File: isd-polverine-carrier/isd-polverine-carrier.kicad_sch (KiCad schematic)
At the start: 0 parts

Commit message: update: isd-polverine-carrier/sch (add battery protection circuit)
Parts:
- added C1: 0.1µF, symbol Device:C
- added C2: 10µF, symbol Device:C
- added F1: Fuse, symbol Device:Fuse
- added J1: BATT, Connector_JST:JST_PH_S2B-PH-K_1x02_P2.00mm_Horizontal, symbol Connector:Conn_01x02_Pin
- added Q1: Q_Dual_NMOS_S1G1D2S2G2D1, Package_SO:TSOP-6_1.65x3.05mm_P0.95mm, symbol Transistor_FET:Q_Dual_NMOS_S1G1D2S2G2D1
- added R1: 0.1k, symbol Device:R
- added R2: 1k, symbol Device:R
- added U1: DW01A, Package_TO_SOT_SMD:SOT-23-6, symbol Battery_Management:DW01A
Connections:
- new net: C1.1, R1.1, U1.5 (VCC)
- new net: R2.1, U1.2 (CS)
- new net: Q1.2 (G), U1.1 (OD)
- new net: Q1.5 (G), U1.3 (OC)
- new net: C1.2, J1.2 (Pin_2), Q1.1 (S), U1.6 (GND)
- new net: Q1.3 (D), Q1.6 (D)
- new net: F1.1, J1.1 (Pin_1)
- new net +BATT: C2.1, F1.2, R1.2
- new net GND: C2.2, Q1.4 (S), R2.2
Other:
- note added: "Battery Protection Circuit"

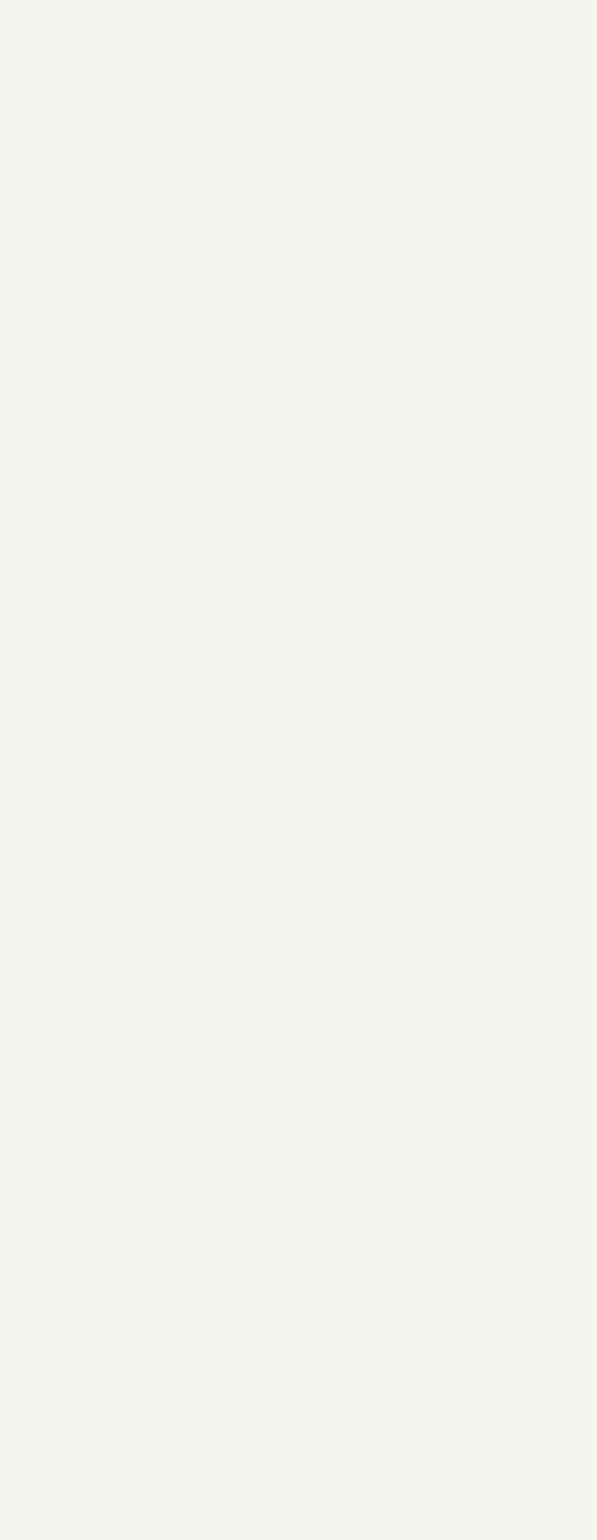
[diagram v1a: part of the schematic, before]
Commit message: Added first charger controller prototype
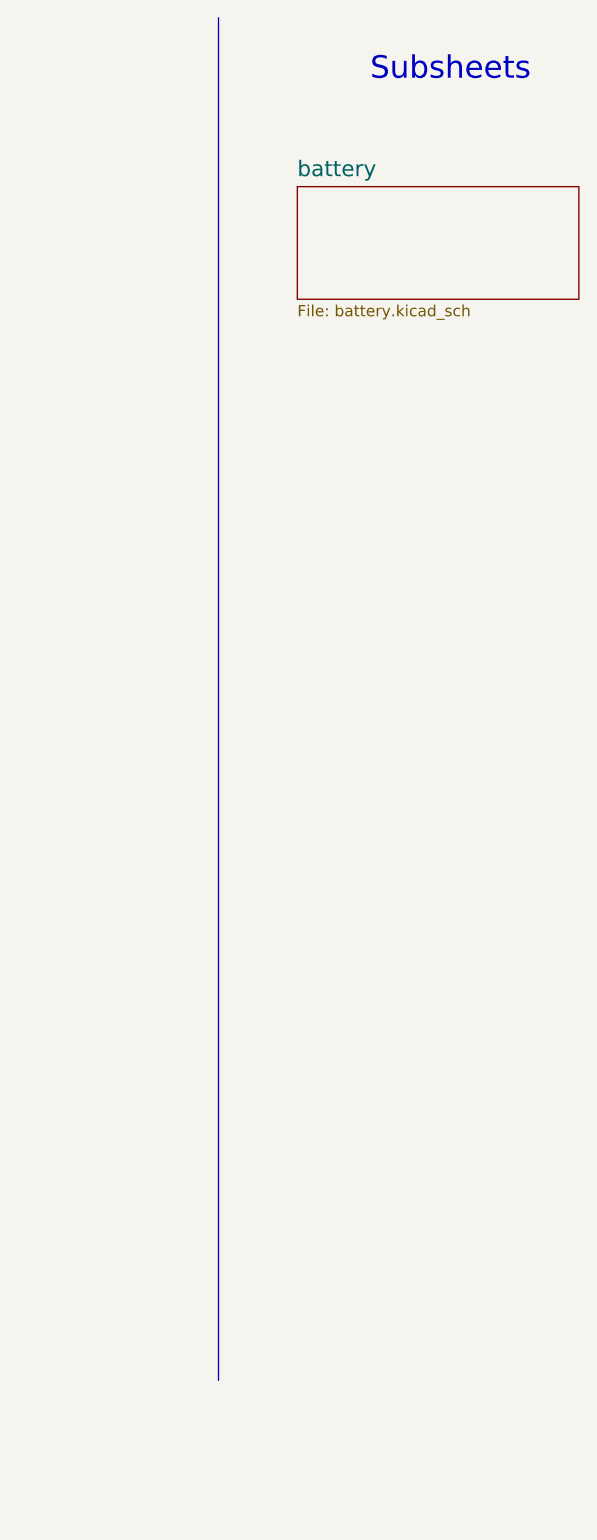
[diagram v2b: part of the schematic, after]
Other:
- added sheet battery (battery.kicad_sch)
- note added: "Subsheets"
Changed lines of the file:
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@@
+		)
+	)
+	(text "Subsheets"
+		(exclude_from_sim no)
+		(at 259.842 18.542 0)
+		(effects
+			(font
+				(size 2.54 2.54)
+			)
 		)
 	)
@@
 		(pts
 			(xy 69.85 173.99) (xy 82.55 173.99)
+		)
+		(stroke
+			(width 0)
+			(type default)
+		)
+	)
+	(polyline
+		(pts
+			(xy 233.68 12.7) (xy 233.68 166.37)
 		)
 		(stroke
@@
 				)
 			)
+		)
+	)
+	(sheet
+		(at 242.57 31.75)
+		(size 31.75 12.7)
+		(exclude_from_sim no)
+		(in_bom yes)
+		(on_board yes)
+		(dnp no)
+		(fields_autoplaced yes)
+		(stroke
+			(width 0.1524)
+			(type solid)
+		)
+		(fill
+			(color 0 0 0 0.0000)
+		)
+		(property "Sheetname" "battery"
+			(at 242.57 30.7844 0)
+			(effects
+				(font
+					(size 1.778 1.778)
+				)
+				(justify left bottom)
+			)
+		)
+		(property "Sheetfile" "battery.kicad_sch"
+			(at 242.57 45.0346 0)
+			(effects
+				(font
+					(size 1.27 1.27)
+				)
+				(justify left top)
+			)
+		)
+		(instances
+			(project "isd-polverine-carrier"
+				(path "/27bbddde-1315-4a7b-91f8-52269d45b0e3"
+					(page "2")
+				)
+			)

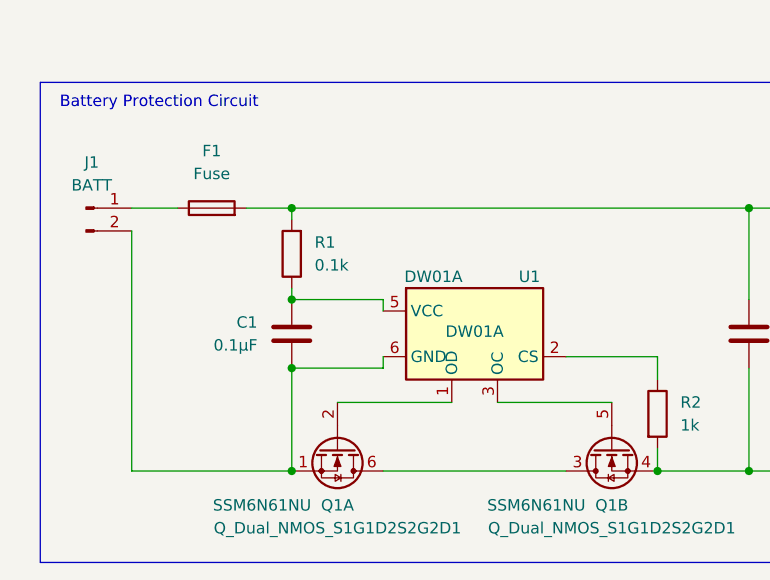
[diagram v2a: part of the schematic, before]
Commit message: update: battery protection circuit (assign components, change to hand-solderable footprints)
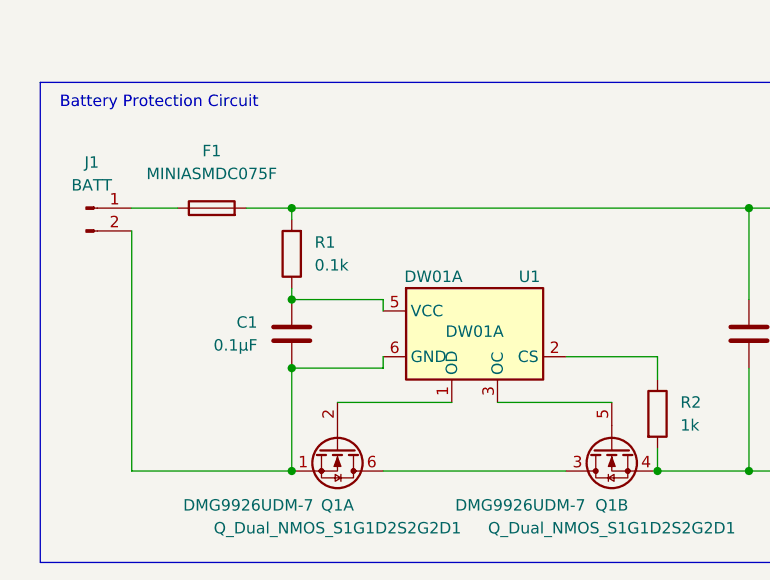
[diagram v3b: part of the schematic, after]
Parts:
- F1: value Fuse -> MINIASMDC075F; footprint (none) -> Fuse:Fuse_1812_4532Metric_Pad1.30x3.40mm_HandSolder; MPU (none) -> MINIASMDC075F/24-2
- Q1: footprint Package_SO:TSOP-6_1.65x3.05mm_P0.95mm -> Package_TO_SOT_SMD:SOT-23-6_Handsoldering; MPN SSM6N61NU -> DMG9926UDM-7
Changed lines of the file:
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@@
 			)
 		)
-		(property "Footprint" "Package_SO:TSOP-6_1.65x3.05mm_P0.95mm"
+		(property "Footprint" "Package_TO_SOT_SMD:SOT-23-6_Handsoldering"
 			(at 52.07 184.15 0)
 			(effects
@@
 			)
 		)
-		(property "Datasheet" "https://www.farnell.com/datasheets/4249053.pdf"
+		(property "Datasheet" "https://www.mouser.fi/datasheet/3/175/1/ds31770.pdf"
 			(at 52.07 184.15 0)
 			(effects
@@
 			)
 		)
-		(property "MPN" "SSM6N61NU"
-			(at 43.688 185.42 90)
+		(property "MPN" "DMG9926UDM-7"
+			(at 42.164 185.42 90)
 			(effects
 				(font
@@
 			)
 		)
-		(property "Footprint" "Package_SO:TSOP-6_1.65x3.05mm_P0.95mm"
+		(property "Footprint" "Package_TO_SOT_SMD:SOT-23-6_Handsoldering"
 			(at 82.55 184.15 0)
 			(effects
@@
 			)
 		)
-		(property "Datasheet" "https://www.farnell.com/datasheets/4249053.pdf"
+		(property "Datasheet" "https://www.mouser.fi/datasheet/3/175/1/ds31770.pdf"
 			(at 82.55 184.15 0)
 			(effects
@@
 			)
 		)
-		(property "MPN" "SSM6N61NU"
-			(at 74.168 185.42 90)
+		(property "MPN" "DMG9926UDM-7"
+			(at 72.39 185.42 90)
 			(effects
 				(font
@@
 			)
 		)
-		(property "Value" "Fuse"
+		(property "Value" "MINIASMDC075F"
 			(at 38.1 148.59 90)
 			(effects
@@
 			)
 		)
-		(property "Footprint" ""
+		(property "Footprint" "Fuse:Fuse_1812_4532Metric_Pad1.30x3.40mm_HandSolder"
 			(at 38.1 154.178 90)
 			(effects
@@
 			)
 		)
-		(property "Datasheet" "~"
+		(property "Datasheet" "https://www.littelfuse.com/assetdocs/littelfuse-ptc-miniasmdc-datasheet"
 			(at 38.1 152.4 0)
 			(effects
@@
 			(effects
 				(font
+					(size 1.27 1.27)
+				)
+				(hide yes)
+			)
+		)
+		(property "MPU" "MINIASMDC075F/24-2"
+			(at 38.1 152.4 90)
+			(effects
+				(font

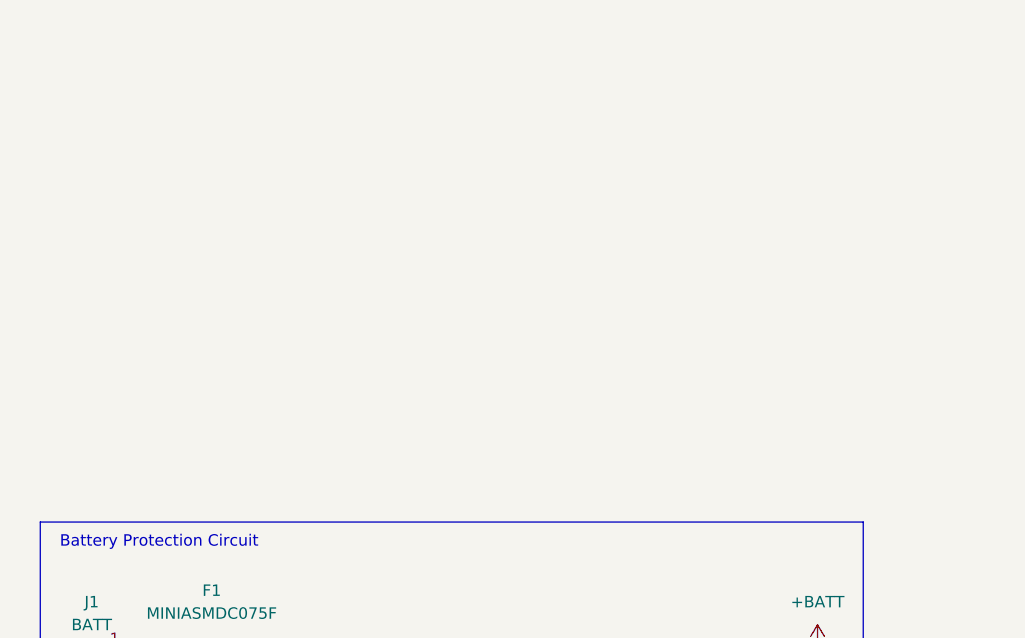
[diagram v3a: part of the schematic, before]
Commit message: add: LDO (3V3)
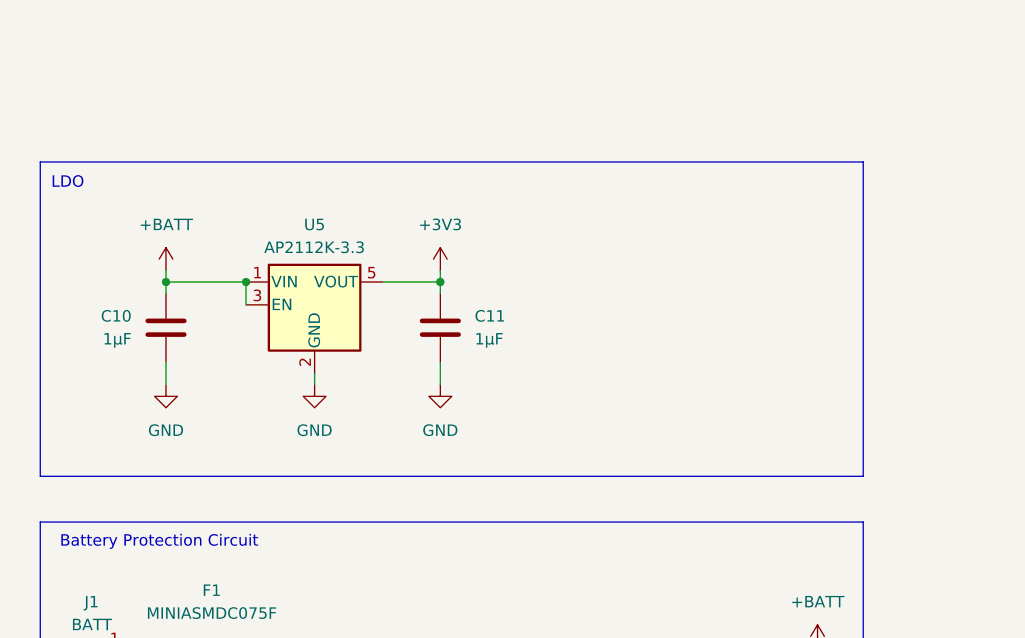
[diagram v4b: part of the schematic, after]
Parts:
- added C10, C11: 1µF, symbol Device:C
- added U5: AP2112K-3.3, Package_TO_SOT_SMD:SOT-23-5_HandSoldering, symbol Regulator_Linear:AP2112K-3.3
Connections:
- net +BATT: now also C10.2, U5.1 (VIN), U5.3 (EN)
- net GND: now also C10.1, C11.2, U5.2 (GND)
- new net +3V3: C11.1, U5.5 (VOUT)
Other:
- note added: "LDO"

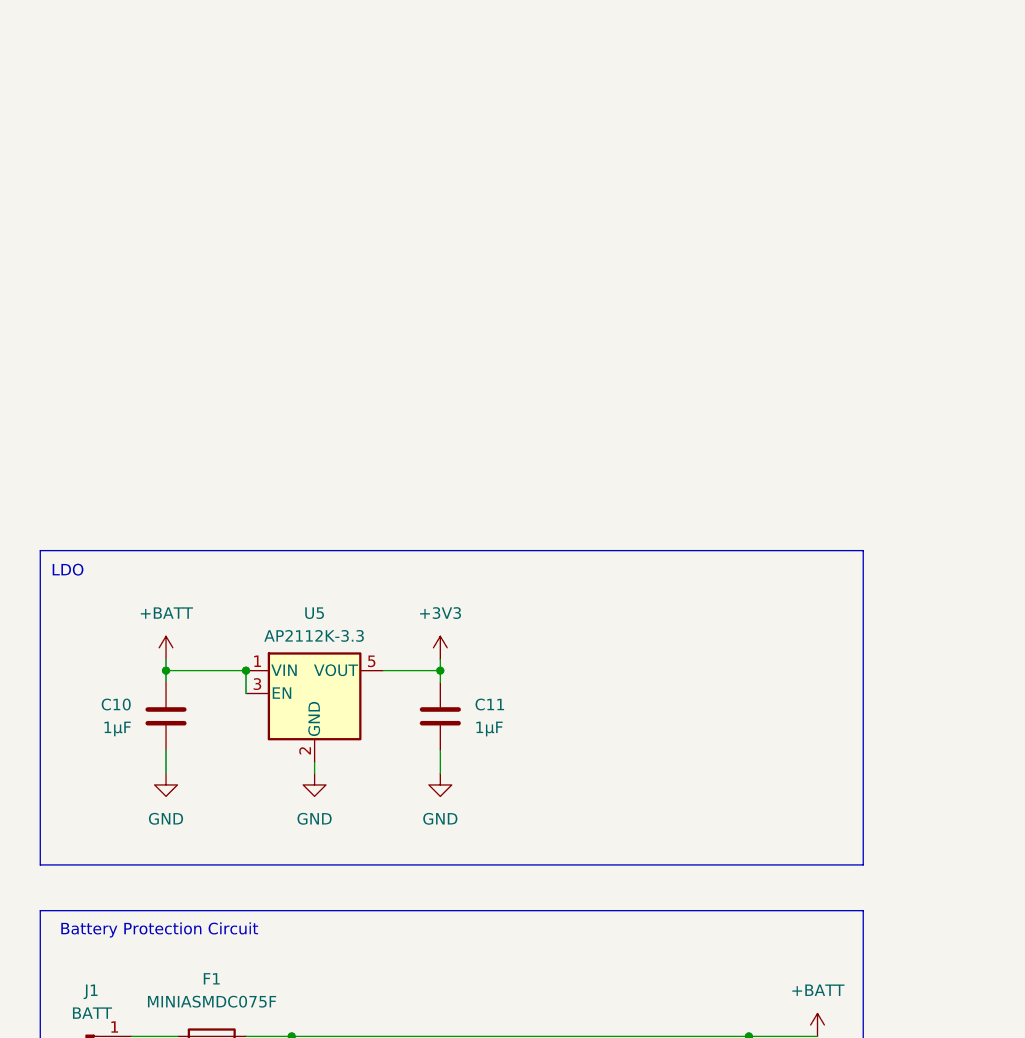
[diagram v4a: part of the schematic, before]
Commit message: add: PV charger (simple, hand-solderable)
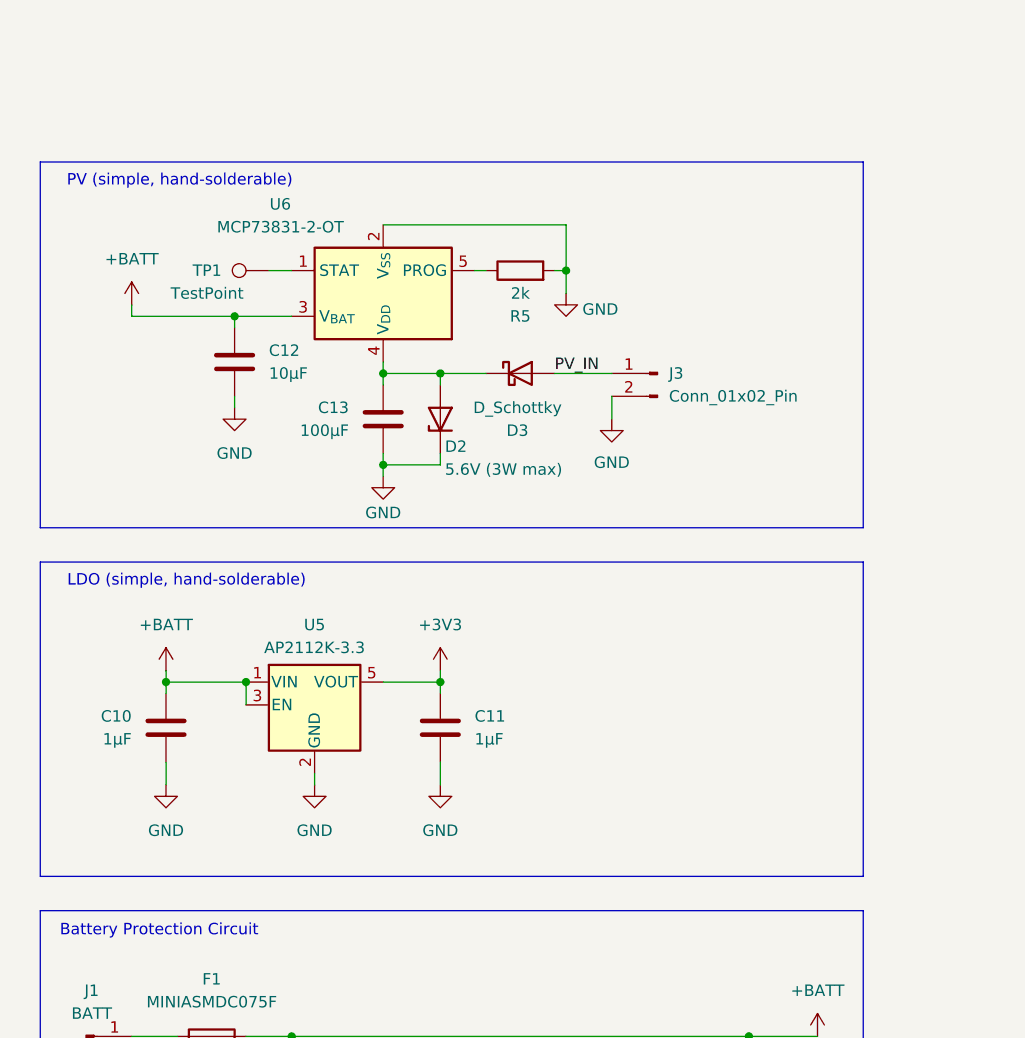
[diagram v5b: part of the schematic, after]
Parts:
- added C12: 10µF, symbol Device:C
- added C13: 100µF, symbol Device:C
- added D2: 5.6V (3W max), Diode_SMD:D_SMB_Handsoldering, symbol Device:D_Zener
- added D3: D_Schottky, symbol Device:D_Schottky
- added J3: Conn_01x02_Pin, Connector_JST:JST_PH_S2B-PH-K_1x02_P2.00mm_Horizontal, symbol Connector:Conn_01x02_Pin
- added R5: 2k, symbol Device:R
- added TP1: TestPoint, symbol Connector:TestPoint
- added U6: MCP73831-2-OT, Package_TO_SOT_SMD:SOT-23-5_HandSoldering, symbol Battery_Management:MCP73831-2-OT
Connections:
- net +BATT: now also C12.1, U6.3 (V_{BAT})
- net GND: now also C12.2, C13.2, D2.1 (K), J3.2 (Pin_2), R5.2, U6.2 (V_{SS})
- new net: C13.1, D2.2 (A), D3.1 (K), U6.4 (V_{DD})
- new net: TP1.1, U6.1 (STAT)
- new net: R5.1, U6.5 (PROG)
- new net PV_IN: D3.2 (A), J3.1 (Pin_1)
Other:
- note added: "LDO (simple, hand-solderable)"
- note added: "PV (simple, hand-solderable)"
- note removed: "LDO"
- moved on the sheet: C10, C11, U5

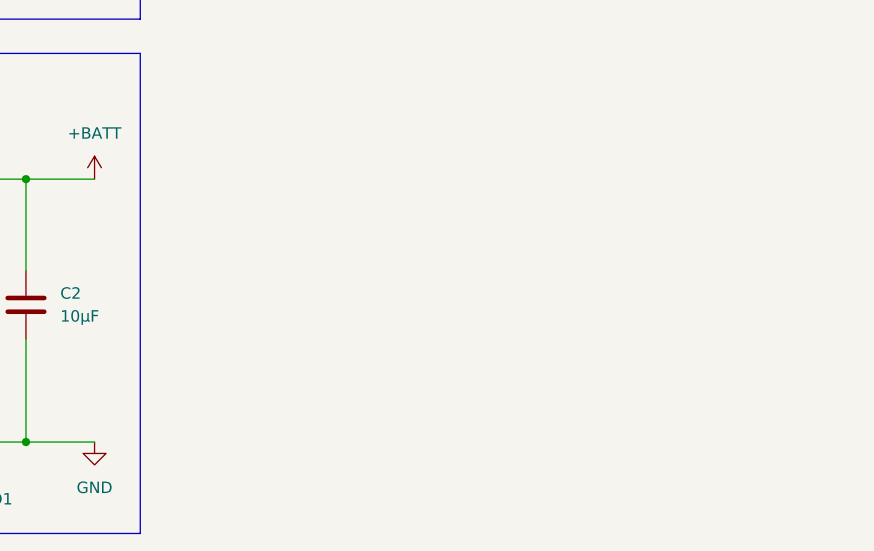
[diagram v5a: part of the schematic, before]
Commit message: add: Polverine mikroBUS headers
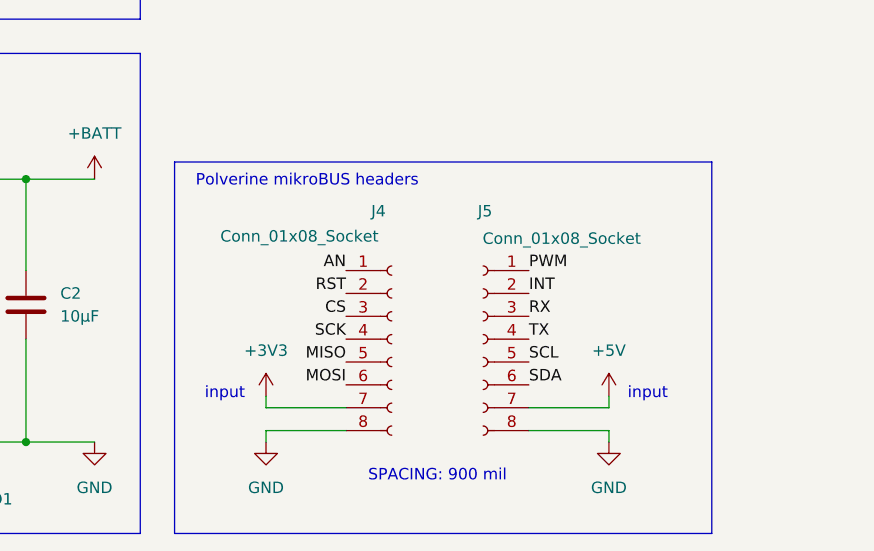
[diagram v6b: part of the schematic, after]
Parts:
- added J4, J5: Conn_01x08_Socket, Connector_PinSocket_2.54mm:PinSocket_1x08_P2.54mm_Vertical, symbol Connector:Conn_01x08_Socket
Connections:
- net +3V3: now also J4.7 (Pin_7)
- net GND: now also J4.8 (Pin_8), J5.8 (Pin_8)
- new net +5V: J5.7 (Pin_7)
- new net AN: J4.1 (Pin_1)
- new net CS: J4.3 (Pin_3)
- new net INT: J5.2 (Pin_2)
- new net MISO: J4.5 (Pin_5)
- new net MOSI: J4.6 (Pin_6)
- new net PWM: J5.1 (Pin_1)
- new net RST: J4.2 (Pin_2)
- new net RX: J5.3 (Pin_3)
- new net SCK: J4.4 (Pin_4)
- new net SCL: J5.5 (Pin_5)
- new net SDA: J5.6 (Pin_6)
- new net TX: J5.4 (Pin_4)
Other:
- note added: "Polverine mikroBUS headers"
- note added: "SPACING: 900 mil"
- note added: "input"
